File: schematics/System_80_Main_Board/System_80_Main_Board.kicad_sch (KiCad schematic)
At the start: 2 parts, among them J1 Expansion, J2 Video Interface

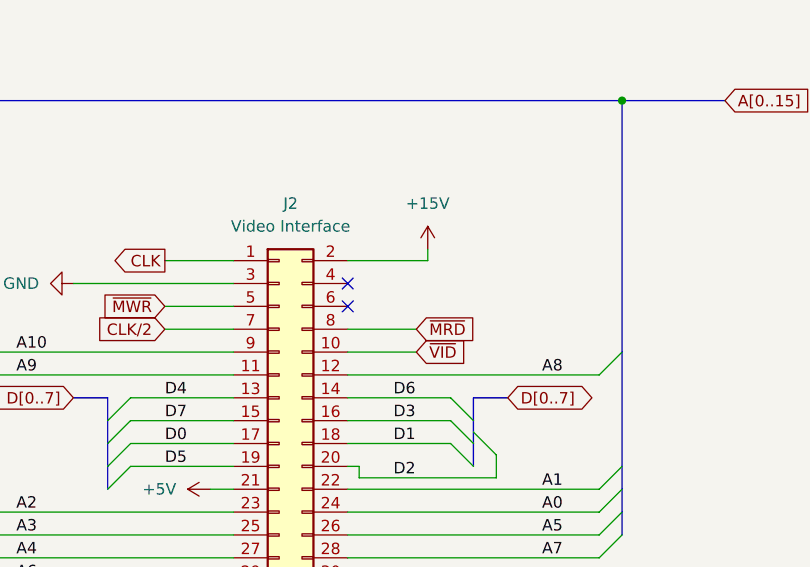
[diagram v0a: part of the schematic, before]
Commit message: Schematic for the System 80 video/cassette board
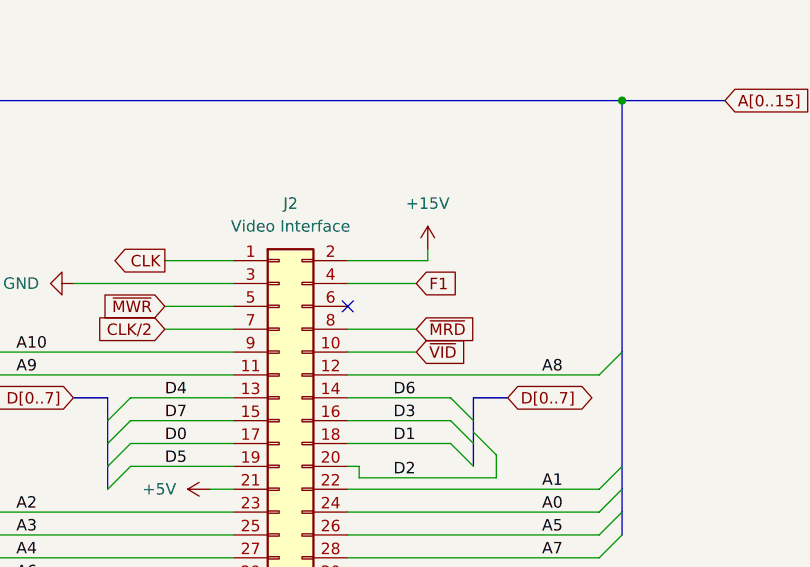
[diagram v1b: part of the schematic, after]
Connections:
- net F1: now reaches J2.4 (Pin_4)
- no-connect marks 7 -> 6
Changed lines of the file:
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@@
-	)
-	(no_connect
-		(at 198.12 99.06)
 	)
 	(no_connect
@@
 		(pts
 			(xy 157.48 132.08) (xy 185.42 132.08)
+		)
+		(stroke
+			(width 0)
+			(type default)
+		)
+	)
+	(wire
+		(pts
+			(xy 205.74 99.06) (xy 198.12 99.06)
 		)
 		(stroke
@@
 			(effects
 				(font
+					(size 1.27 1.27)
+				)
+				(justify left)
+				(hide yes)
+			)
+		)
+	)
+	(global_label "F1"
+		(shape input)
+		(at 205.74 99.06 0)
+		(fields_autoplaced yes)
+		(effects
+			(font
+				(size 1.27 1.27)
+			)
+			(justify left)
+		)
+		(property "Intersheetrefs" "${INTERSHEET_REFS}"
+			(at 211.0233 99.06 0)
+			(effects
+				(font

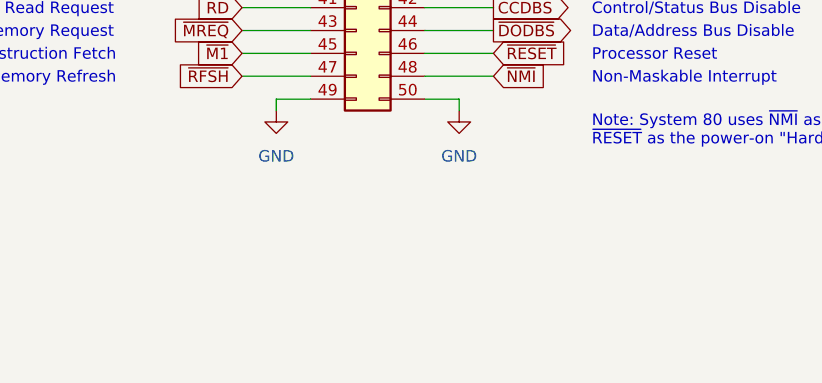
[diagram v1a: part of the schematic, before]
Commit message: Diagram showing the arrangement of pins on the expansion edge connector
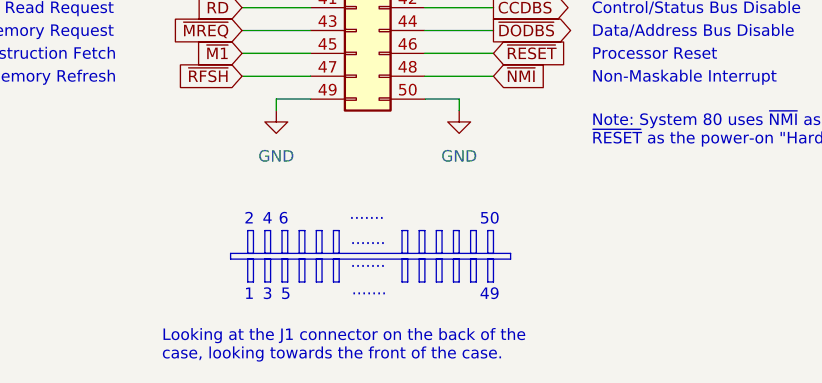
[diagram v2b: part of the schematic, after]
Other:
- note added: "......."
- note added: "1"
- note added: "2"
- note added: "3"
- note added: "4"
- note added: "49"
- note added: "5"
- note added: "50"
- note added: "6"
- note added: "Looking at the J1 connector on the back of the case, looking towards the front of the case."
